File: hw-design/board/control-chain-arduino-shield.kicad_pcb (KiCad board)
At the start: 2 copper layers, 68.6 x 53.3 mm, 35 parts, among them J1 CC_MAIN, J2 CC_NEXT, P1 Power, P10 Power, P11 Analog, P12 Digital, P13 Digital, P2 Analog, P3 Digital, P4 Digital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

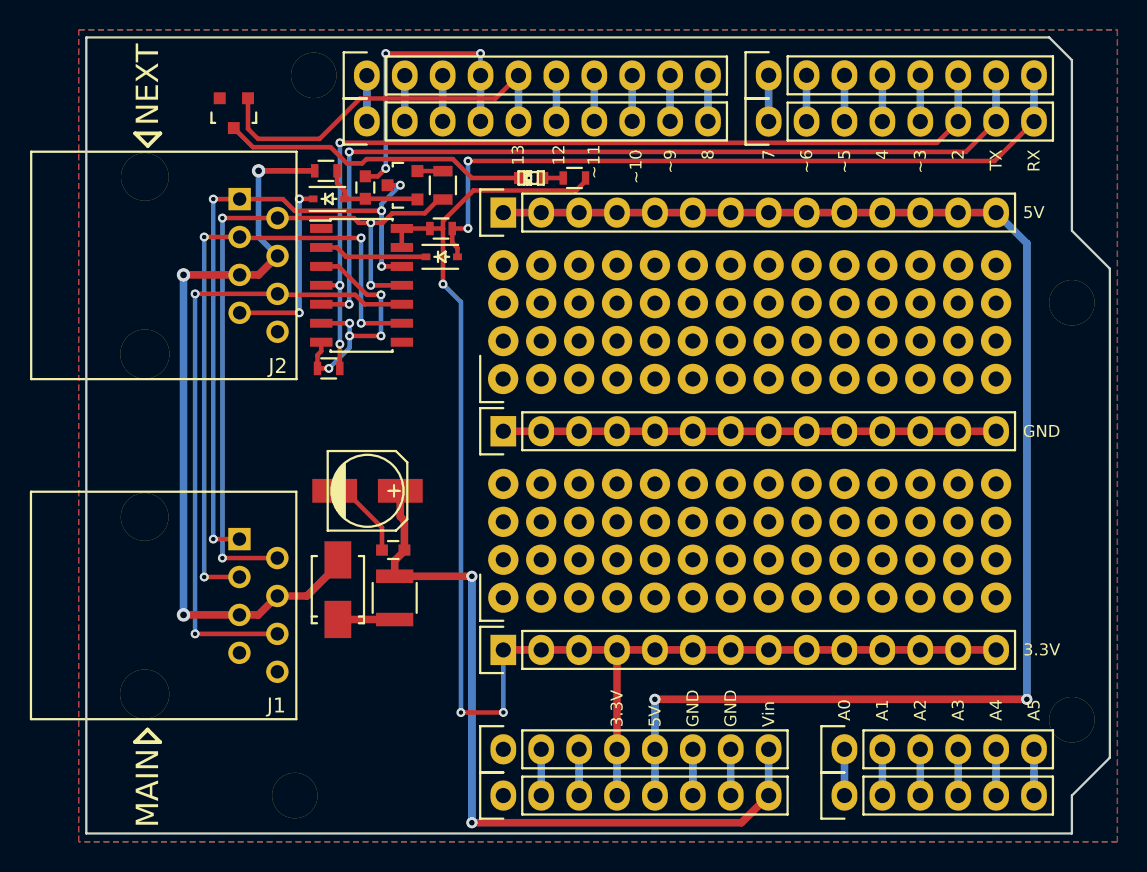
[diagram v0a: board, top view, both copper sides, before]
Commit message: add enable circuit for RE pin
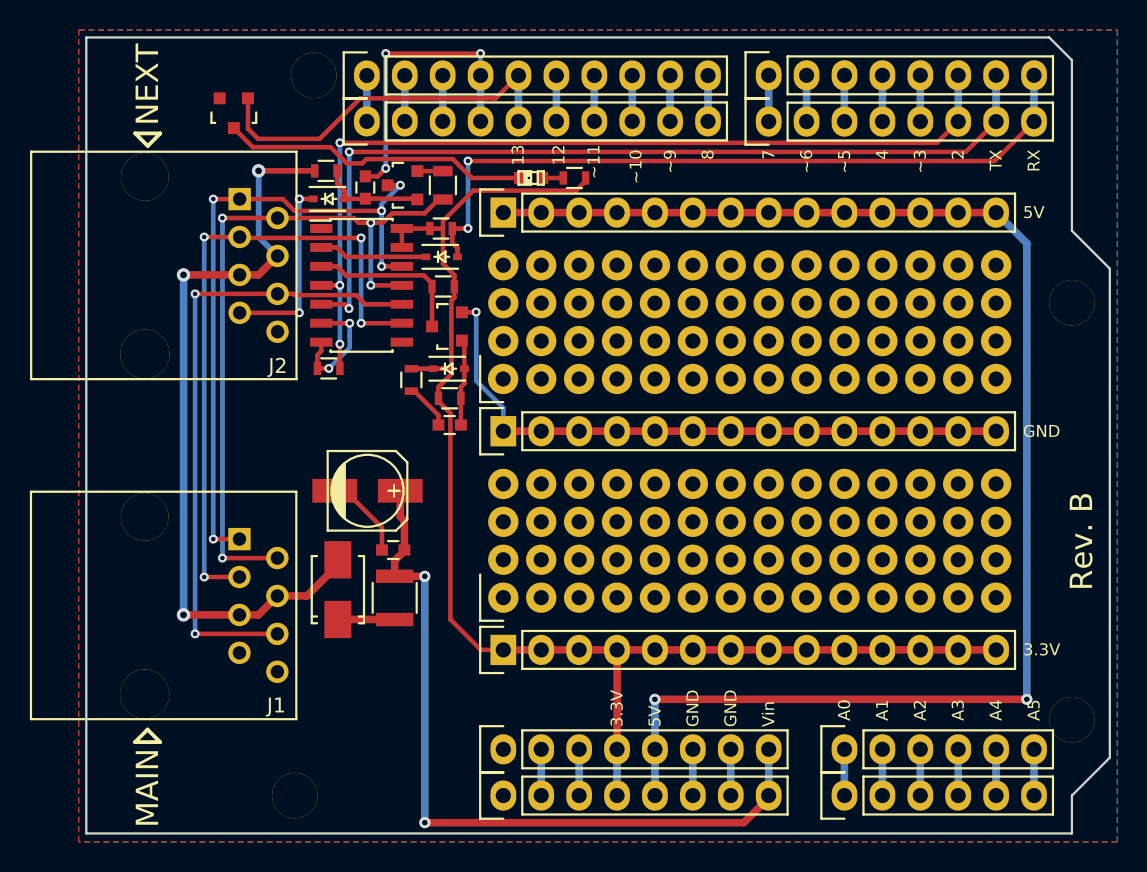
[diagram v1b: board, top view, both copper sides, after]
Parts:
- added C4: 10uF, Capacitors_SMD:C_0603, F.Cu at (135.3, 99.0)
- added D5: 1N4148, Diodes_SMD:SOD-323, F.Cu at (135.3, 95.2)
- added Q2: 2N7002, Housings_SOT-23_SOT-143_TSOT-6:SOT-23, F.Cu at (135.2, 92.4)
- added R2: 10K, Resistors_SMD:R_0603, F.Cu at (132.8, 96.0)
- added R3: 220K, Resistors_SMD:R_0603, F.Cu at (135.3, 97.2)
- added R4: 10K, Resistors_SMD:R_0603, F.Cu at (134.9, 89.7)
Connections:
- P1 pad 1: (no net) -> Net-(P1-Pad1)
- P10 pad 1: (no net) -> Net-(P10-Pad1)
- U1 pad 3: GNDD -> RE
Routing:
- net RE: track 0.00 -> 10.8 mm
- net Net-(C4-Pad1): track 0.00 -> 5.82 mm
- net +3V3: track 98.4 -> 92.8 mm, vias 3 -> 0
- net GNDD: track 82.9 -> 86.1 mm, vias 8 -> 6
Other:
- board text added: "Rev. B"

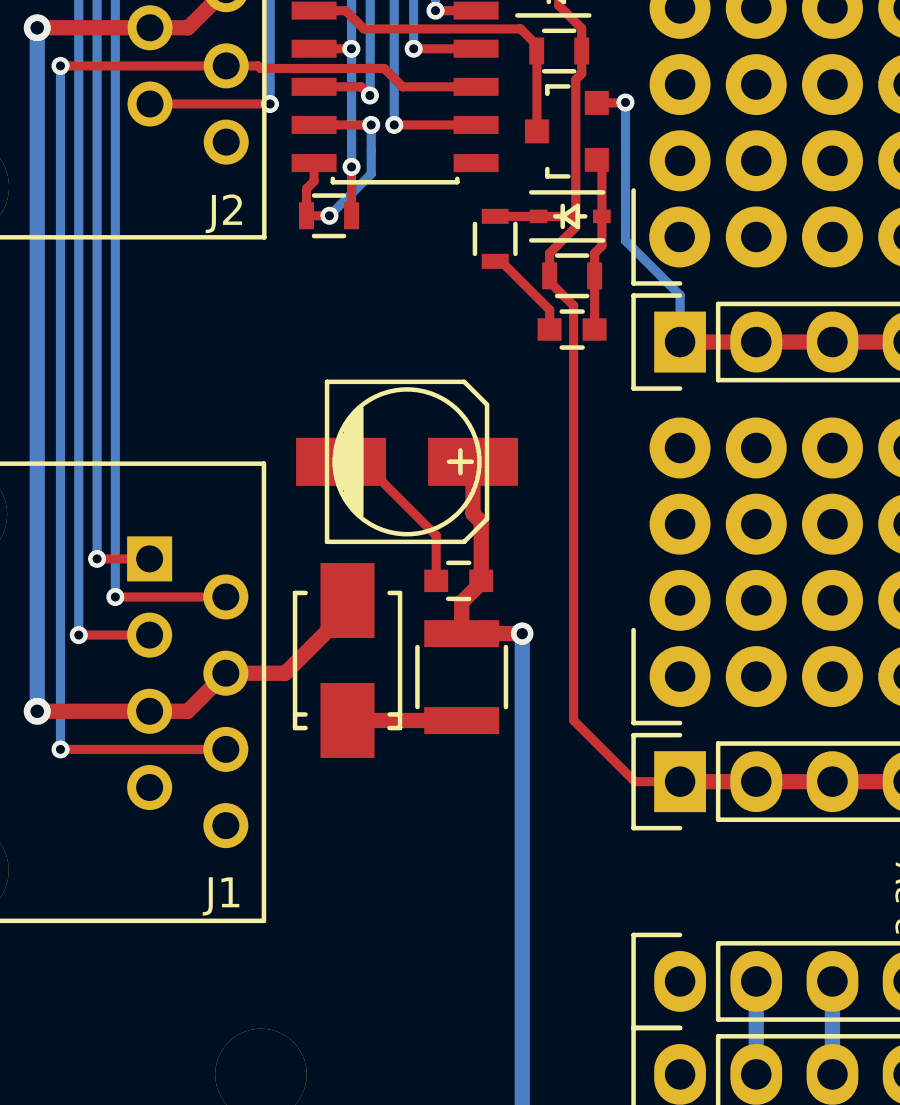
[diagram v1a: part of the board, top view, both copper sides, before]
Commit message: update footprints (remove silkscreen from pads)
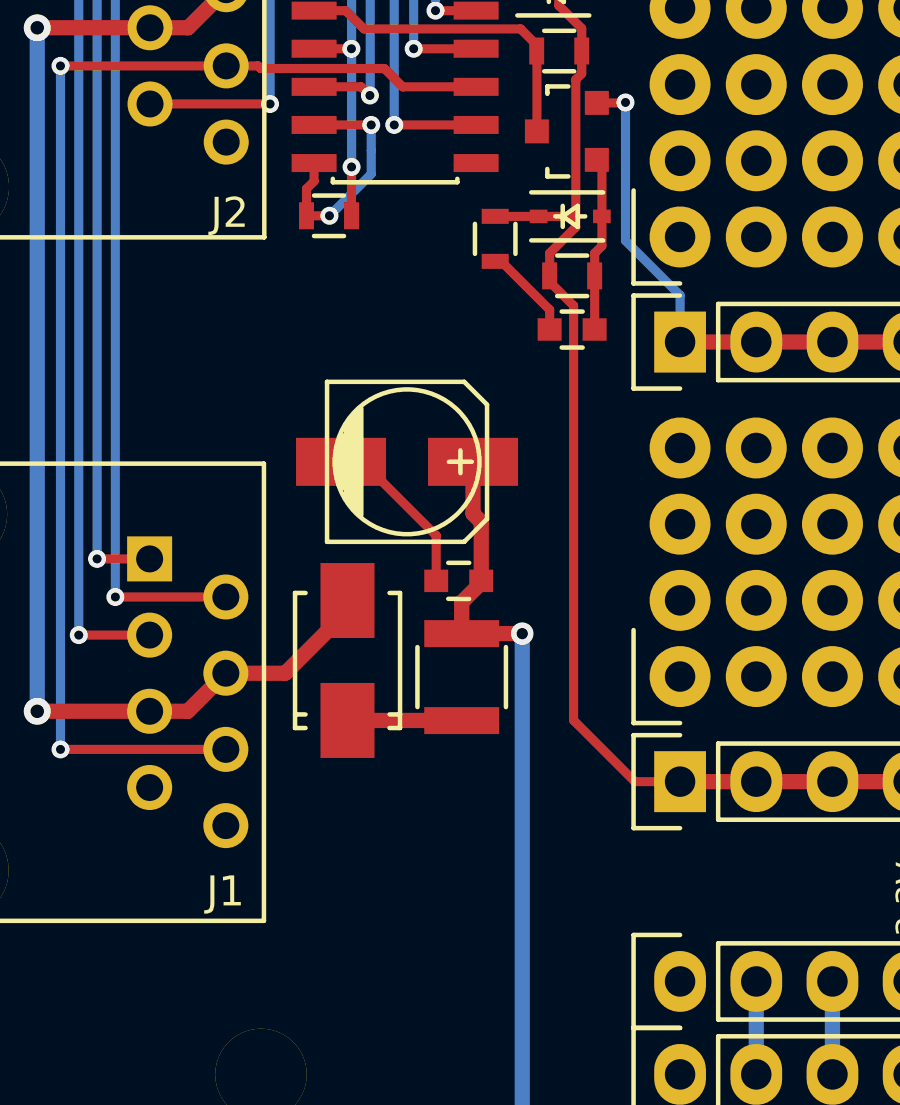
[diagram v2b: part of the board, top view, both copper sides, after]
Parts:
- P19, P20, P21: footprint Pin_Headers:Pin_Header_Straight_1x14 -> local-footprints:Pin_Header_Straight_1x14

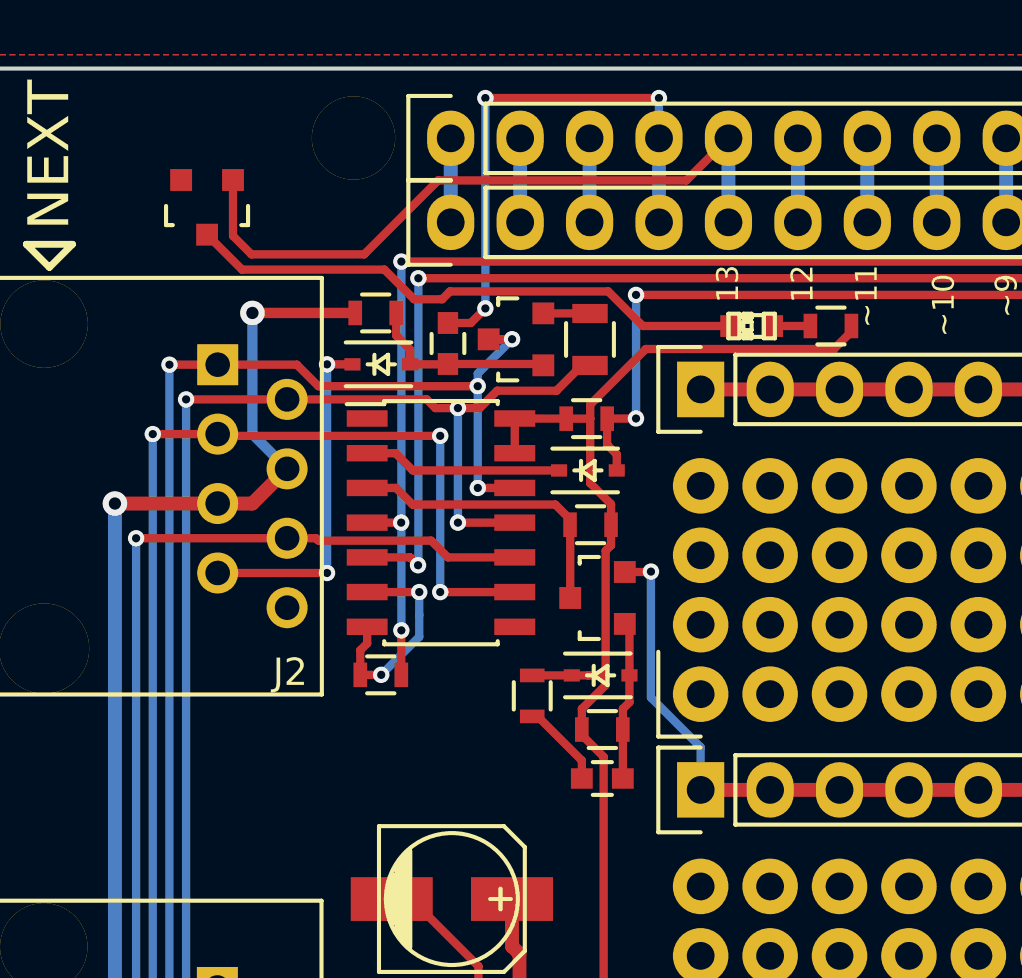
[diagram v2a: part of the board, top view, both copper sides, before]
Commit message: move led position
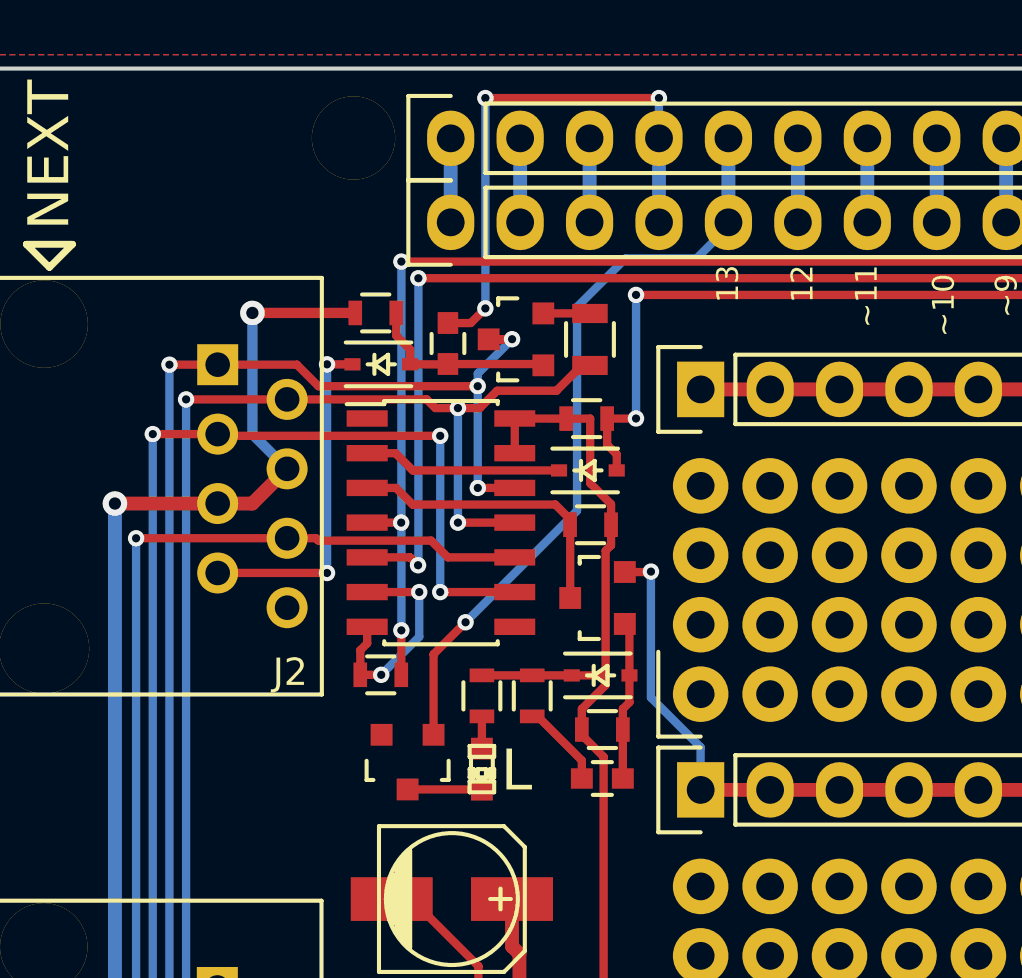
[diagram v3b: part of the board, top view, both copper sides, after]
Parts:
- moved Q1 21.6 mm to (128.2, 98.4)
- moved D2 19.0 mm to (130.9, 98.7), turned to 90 degrees
- moved R1 18.6 mm to (130.9, 96.0), turned to 270 degrees
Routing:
- net Net-(D2-Pad1): track 20.8 -> 2.72 mm
- net +3V3: track 92.8 -> 83.2 mm
- net IO13/SCK: track 25.3 -> 27.8 mm, vias 0 -> 1
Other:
- board text added: "L"

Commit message: update gerber and pdf files
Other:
- board text added: "IOREF"
- board text added: "RESET"
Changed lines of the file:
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@@
     (area 110.922999 72.949999 179.653001 126.440001)
     (thickness 1.6)
-    (drawings 66)
+    (drawings 68)
     (tracks 309)
     (zones 0)
@@
     (visible_elements FFFFFF7F)
     (pcbplotparams
-      (layerselection 0x3d0f0_80000001)
+      (layerselection 0x310f0_80000001)
       (usegerberextensions false)
       (excludeedgelayer true)
@@
     )
   )
+  (gr_text IOREF (at 141.47546 119.31602 90) (layer F.SilkS)
+    (effects (font (size 0.8 0.8) (thickness 0.1)) (justify left))
+  )
+  (gr_text RESET (at 144.01546 119.31602 90) (layer F.SilkS)
+    (effects (font (size 0.8 0.8) (thickness 0.1)) (justify left))
+  )
   (gr_text L (at 132.20446 98.70392) (layer F.SilkS)
